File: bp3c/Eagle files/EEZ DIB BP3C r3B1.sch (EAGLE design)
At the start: 56 parts, among them IC1 TCA9534PWR, Q1 2N7002, Q2 2N7002, Q3 2N7002, Q4 2N7002, X1 ZL202-20G, X2 ZL202-20G, X3 ZL202-20G, X4 ZL212-40KG, X5 ZL262-28DG, X6 ZL262-28DG, X7 ZL262-28DG

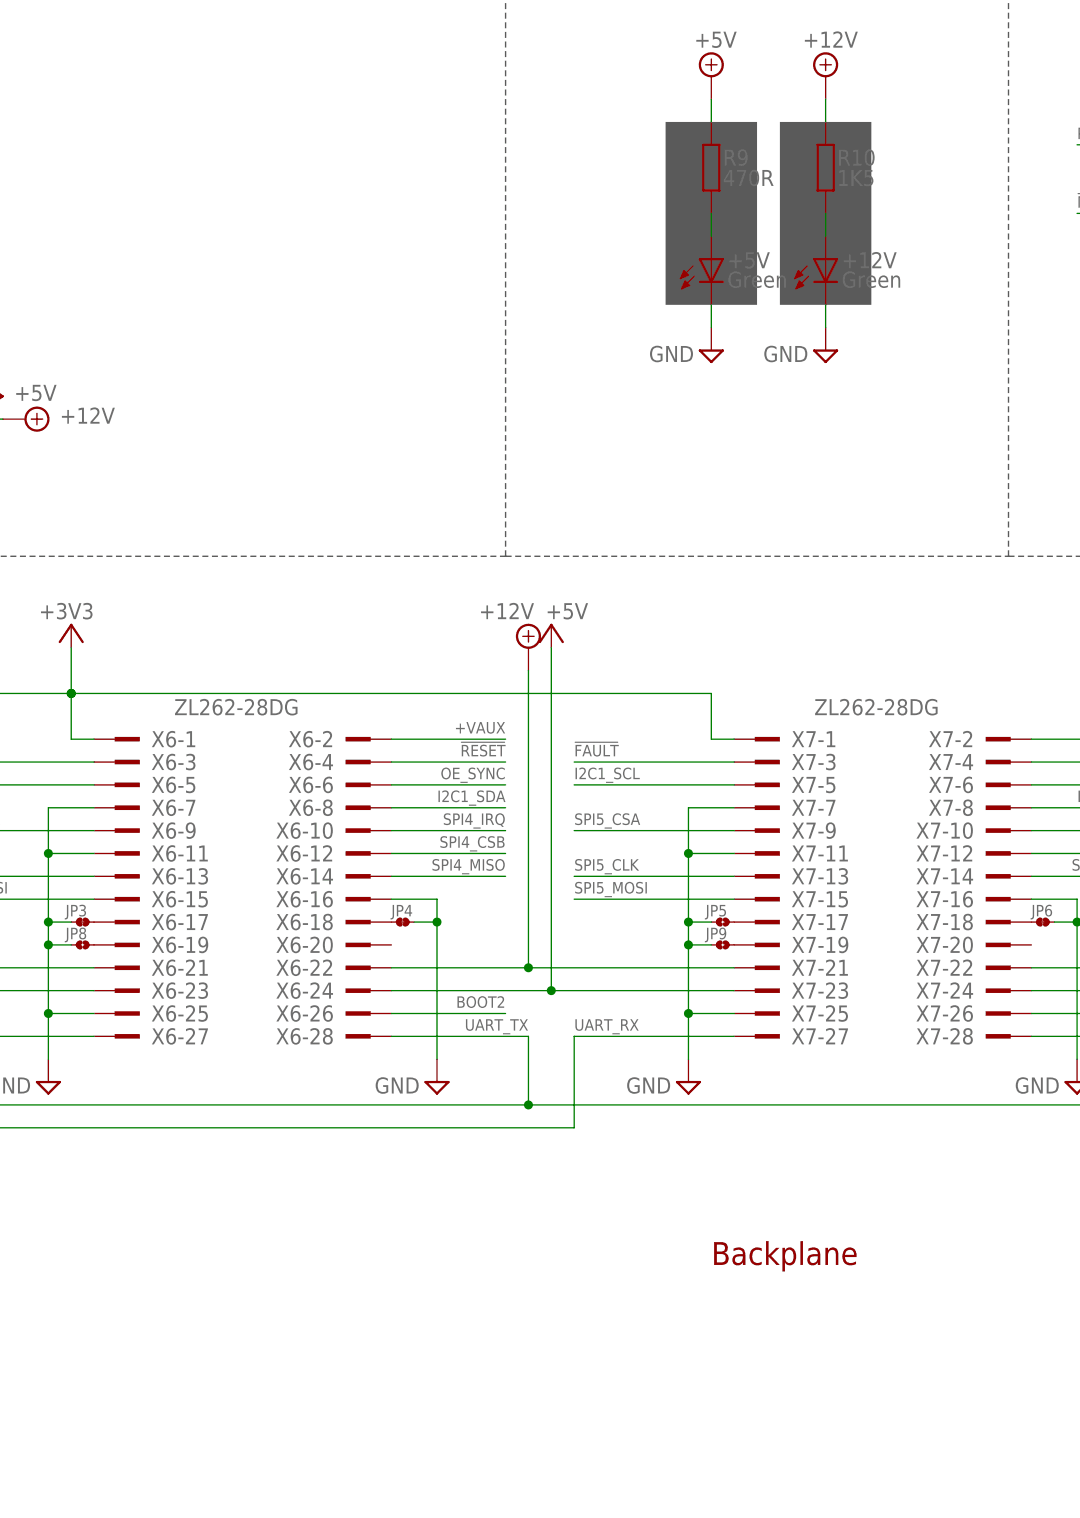
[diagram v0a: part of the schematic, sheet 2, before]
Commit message: BP3C BOM update, optional X8
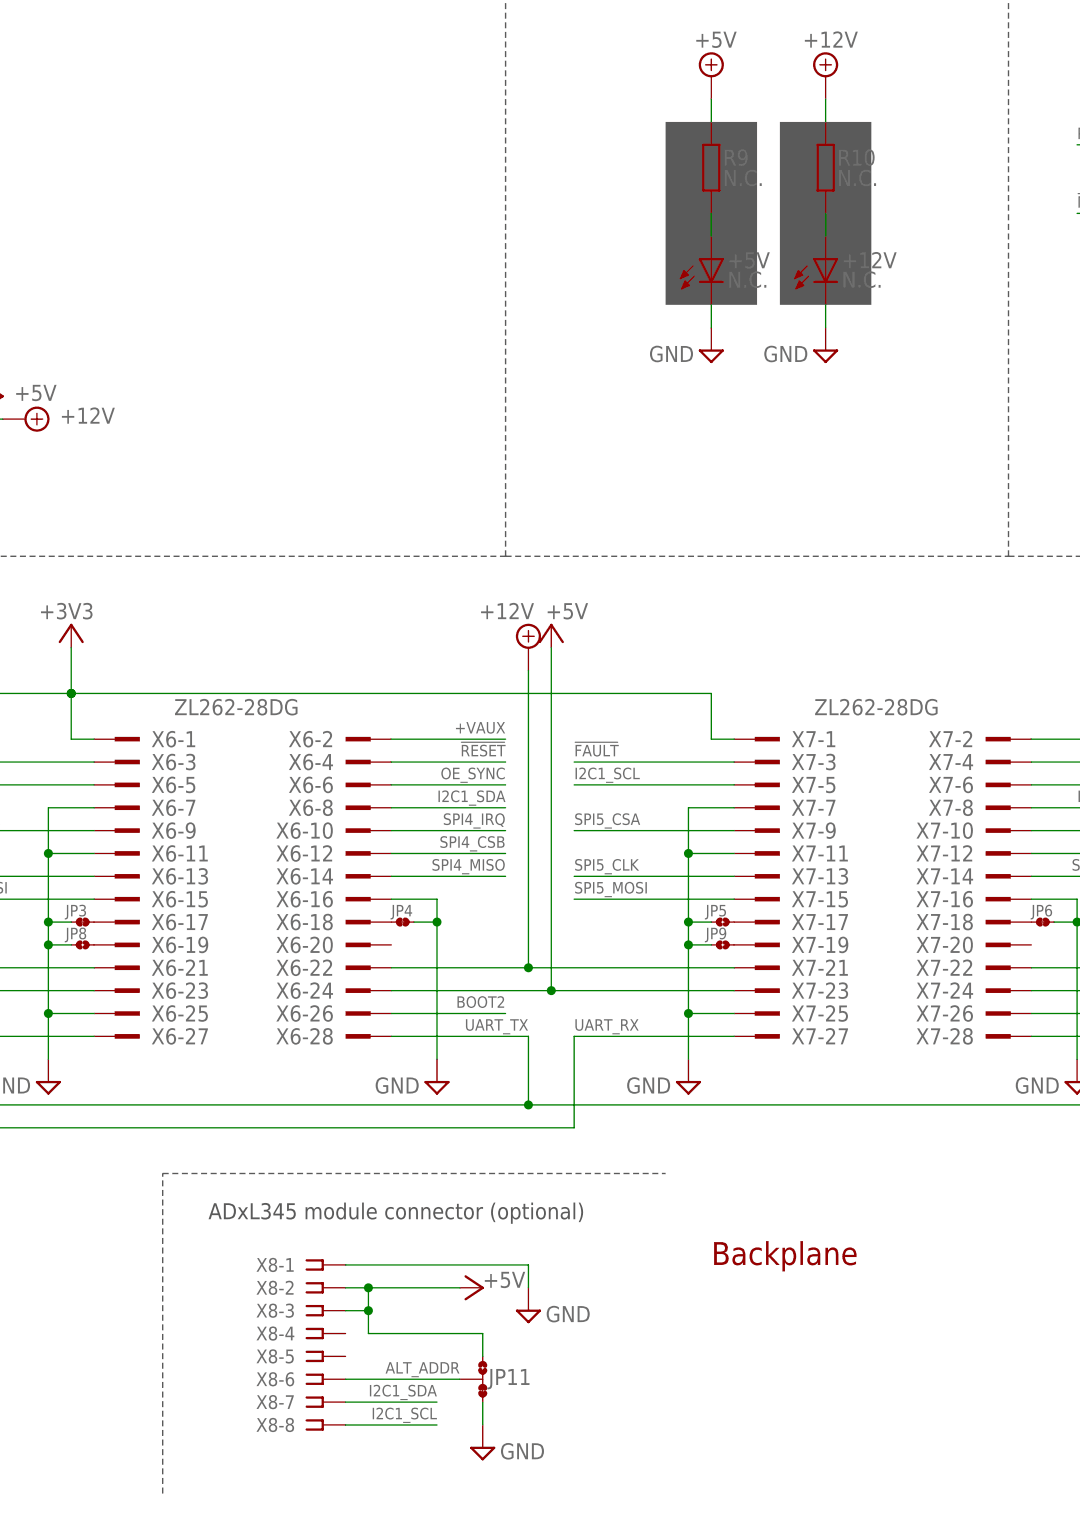
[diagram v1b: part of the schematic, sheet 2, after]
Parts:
- added JP11: JP3-CUT, EEZ_Lib1:JP3-CUT
- added X8: N.C., con-samtec:SSW-108-02-S-S
- +12V, +5V, CGND, SRAIL: value Green -> N.C.
- PAR: value Yellow -> N.C.
- R1, R3, R5, R7: value 330R -> N.C.
- R10: value 1K5 -> N.C.
- R9: value 470R -> N.C.
- SER: value Red -> N.C.
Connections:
- new net ALT_ADDR: JP11.COM, X8-6.1
- net +5V: now also JP11.NO, X8-2.1, X8-3.1
- net GND: now also JP11.NC, X8-1.1
- net I2C1_SCL: now also X8-8.1
- net I2C1_SDA: now also X8-7.1
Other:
- note added: "ADxL345 module connector (optional)"
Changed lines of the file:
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@@
 <part name="P+1" library="supply1" deviceset="+5V" device=""/>
 <part name="P+2" library="supply1" deviceset="+5V" device=""/>
-<part name="SER" library="EEZ_Lib1" deviceset="LED" device="0805" value="Red"/>
-<part name="PAR" library="EEZ_Lib1" deviceset="LED" device="0805" value="Yellow"/>
-<part name="R3" library="rcl" deviceset="R-EU_" device="R0805" value="330R"/>
-<part name="R5" library="rcl" deviceset="R-EU_" device="R0805" value="330R"/>
+<part name="SER" library="EEZ_Lib1" deviceset="LED" device="0805" value="N.C."/>
+<part name="PAR" library="EEZ_Lib1" deviceset="LED" device="0805" value="N.C."/>
+<part name="R3" library="rcl" deviceset="R-EU_" device="R0805" value="N.C."/>
+<part name="R5" library="rcl" deviceset="R-EU_" device="R0805" value="N.C."/>
 <part name="X1" library="EEZ_connectors" deviceset="DS1021-2*10SF11" device="" value="ZL202-20G"/>
 <part name="X2" library="EEZ_connectors" deviceset="DS1021-2*10SF11" device="" value="ZL202-20G"/>
 <part name="X3" library="EEZ_connectors" deviceset="DS1021-2*10SF11" device="" value="ZL202-20G"/>
 <part name="X4" library="EEZ_connectors" deviceset="ZL212-40KG" device=""/>
-<part name="+5V" library="EEZ_Lib1" deviceset="LED" device="0805" value="Green"/>
-<part name="R9" library="rcl" deviceset="R-EU_" device="R0805" value="470R"/>
-<part name="+12V" library="EEZ_Lib1" deviceset="LED" device="0805" value="Green"/>
-<part name="R10" library="rcl" deviceset="R-EU_" device="R0805" value="1K5"/>
+<part name="+5V" library="EEZ_Lib1" deviceset="LED" device="0805" value="N.C."/>
+<part name="R9" library="rcl" deviceset="R-EU_" device="R0805" value="N.C."/>
+<part name="+12V" library="EEZ_Lib1" deviceset="LED" device="0805" value="N.C."/>
+<part name="R10" library="rcl" deviceset="R-EU_" device="R0805" value="N.C."/>
 <part name="SUPPLY3" library="supply2" deviceset="+12V" device=""/>
 <part name="SUPPLY32" library="supply2" deviceset="+5V" device=""/>
@@
 <part name="R2" library="rcl" deviceset="R-EU_" device="R0805" value="100K"/>
 <part name="P+3" library="supply1" deviceset="+5V" device=""/>
-<part name="CGND" library="EEZ_Lib1" deviceset="LED" device="0805" value="Green"/>
-<part name="R1" library="rcl" deviceset="R-EU_" device="R0805" value="330R"/>
+<part name="CGND" library="EEZ_Lib1" deviceset="LED" device="0805" value="N.C."/>
+<part name="R1" library="rcl" deviceset="R-EU_" device="R0805" value="N.C."/>
 <part name="K_SRAIL" library="EEZ_Lib1" deviceset="RELAY_RT314012" device="-2" value="RT424005"/>
 <part name="D6" library="EEZ_Lib1" deviceset="DIODE" device="SOD323R" value="BAS316"/>
@@
 <part name="R8" library="rcl" deviceset="R-EU_" device="R0805" value="100K"/>
 <part name="P+8" library="supply1" deviceset="+5V" device=""/>
-<part name="SRAIL" library="EEZ_Lib1" deviceset="LED" device="0805" value="Green"/>
-<part name="R7" library="rcl" deviceset="R-EU_" device="R0805" value="330R"/>
+<part name="SRAIL" library="EEZ_Lib1" deviceset="LED" device="0805" value="N.C."/>
+<part name="R7" library="rcl" deviceset="R-EU_" device="R0805" value="N.C."/>
 <part name="D4" library="EEZ_Lib1" deviceset="DIODE" device="SOD323R" value="N.C."/>
 <part name="D3" library="EEZ_Lib1" deviceset="DIODE" device="SOD323R" value="N.C."/>
@@
 <part name="R11" library="rcl" deviceset="R-EU_" device="R0805" value="10K"/>
 <part name="+3V4" library="supply1" deviceset="+3V3" device=""/>
+<part name="X8" library="con-samtec" deviceset="SSW-108-02-S-S" device="" value="N.C."/>
+<part name="SUPPLY20" library="supply2" deviceset="GND" device=""/>
+<part name="P+11" library="supply1" deviceset="+5V" device=""/>
+<part name="JP11" library="EEZ_Lib1" deviceset="JP3-CUT" device=""/>
+<part name="SUPPLY21" library="supply2" deviceset="GND" device=""/>
 </parts>
 <sheets>
@@
 <vertex x="98.425" y="165.1"/>
 <vertex x="104.775" y="165.1"/>
-<vertex x="102.235" y="146.05"/>
+<vertex x="104.775" y="146.05"/>
 <vertex x="88.9" y="146.05"/>
 </polygon>
@@
 <wire x1="198.12" y1="106.68" x2="198.12" y2="177.8" width="0.1524" layer="97" style="shortdash"/>
 <text x="205.74" y="175.26" size="1.778" layer="97">Peripheral modules RESET</text>
+<wire x1="104.14" y1="38.1" x2="160.02" y2="38.1" width="0.1524" layer="97" style="shortdash"/>
+<wire x1="104.14" y1="2.54" x2="104.14" y2="38.1" width="0.1524" layer="97" style="shortdash"/>
+<text x="109.22" y="33.02" size="1.778" layer="97">ADxL345 module connector (optional)</text>
 </plain>
 <instances>
@@
 <attribute name="VALUE" x="230.505" y="172.72" size="1.778" layer="96" rot="MR180"/>
 </instance>
+<instance part="X8" gate="-1" x="121.92" y="27.94" smashed="yes">
+<attribute name="NAME" x="118.872" y="28.702" size="1.524" layer="95" rot="R180"/>
+</instance>
+<instance part="X8" gate="-2" x="121.92" y="25.4" smashed="yes">
+<attribute name="NAME" x="118.872" y="26.162" size="1.524" layer="95" rot="R180"/>
+</instance>
+<instance part="X8" gate="-3" x="121.92" y="22.86" smashed="yes">
+<attribute name="NAME" x="118.872" y="23.622" size="1.524" layer="95" rot="R180"/>
+</instance>
+<instance part="X8" gate="-4" x="121.92" y="20.32" smashed="yes">
+<attribute name="NAME" x="118.872" y="21.082" size="1.524" layer="95" rot="R180"/>
+</instance>
+<instance part="X8" gate="-5" x="121.92" y="17.78" smashed="yes">
+<attribute name="NAME" x="118.872" y="18.542" size="1.524" layer="95" rot="R180"/>
+</instance>
+<instance part="X8" gate="-6" x="121.92" y="15.24" smashed="yes">
+<attribute name="NAME" x="118.872" y="16.002" size="1.524" layer="95" rot="R180"/>
+</instance>
+<instance part="X8" gate="-7" x="121.92" y="12.7" smashed="yes">
+<attribute name="NAME" x="118.872" y="13.462" size="1.524" layer="95" rot="R180"/>
+</instance>
+<instance part="X8" gate="-8" x="121.92" y="10.16" smashed="yes">
+<attribute name="NAME" x="118.872" y="10.922" size="1.524" layer="95" rot="R180"/>
+</instance>
+<instance part="SUPPLY20" gate="GND" x="144.78" y="22.86" smashed="yes" rot="MR0">
+<attribute name="VALUE" x="146.685" y="21.59" size="1.778" layer="96"/>
+</instance>
+<instance part="P+11" gate="1" x="139.7" y="25.4" smashed="yes" rot="R270">
+<attribute name="VALUE" x="139.7" y="25.4" size="1.778" layer="96"/>
+</instance>
+<instance part="JP11" gate="G$1" x="139.7" y="15.24" smashed="yes" rot="MR0">
+<attribute name="NAME" x="140.335" y="14.605" size="1.778" layer="95"/>
+</instance>
+<instance part="SUPPLY21" gate="GND" x="139.7" y="7.62" smashed="yes" rot="MR0">
+<attribute name="VALUE" x="141.605" y="6.35" size="1.778" layer="96"/>
+</instance>
 </instances>
 <busses>
@@
 <pinref part="X5" gate="-16" pin="1"/>
 </segment>
+<segment>
+<pinref part="X8" gate="-1" pin="1"/>
+<wire x1="124.46" y1="27.94" x2="144.78" y2="27.94" width="0.1524" layer="91"/>
+<pinref part="SUPPLY20" gate="GND" pin="GND"/>
+<wire x1="144.78" y1="25.4" x2="144.78" y2="27.94" width="0.1524" layer="91"/>
+</segment>
+<segment>
+<pinref part="SUPPLY21" gate="GND" pin="GND"/>
+<pinref part="JP11" gate="G$1" pin="NC"/>
+<wire x1="139.7" y1="10.16" x2="139.7" y2="12.7" width="0.1524" layer="91"/>
+</segment>
 </net>
 <net name="+3V3" class="0">
@@
 <pinref part="X7" gate="-24" pin="1"/>
 </segment>
+<segment>
+<pinref part="X8" gate="-2" pin="1"/>
+<wire x1="124.46" y1="25.4" x2="127" y2="25.4" width="0.1524" layer="91"/>
+<pinref part="P+11" gate="1" pin="+5V"/>
+<pinref part="X8" gate="-3" pin="1"/>
+<wire x1="127" y1="25.4" x2="137.16" y2="25.4" width="0.1524" layer="91"/>
+<wire x1="124.46" y1="22.86" x2="127" y2="22.86" width="0.1524" layer="91"/>
+<wire x1="127" y1="22.86" x2="127" y2="25.4" width="0.1524" layer="91"/>
+<junction x="127" y="25.4"/>
+<pinref part="JP11" gate="G$1" pin="NO"/>
+<wire x1="139.7" y1="17.78" x2="139.7" y2="20.32" width="0.1524" layer="91"/>
+<wire x1="139.7" y1="20.32" x2="127" y2="20.32" width="0.1524" layer="91"/>
+<wire x1="127" y1="20.32" x2="127" y2="22.86" width="0.1524" layer="91"/>
+<junction x="127" y="22.86"/>
+</segment>
 </net>
 <net name="+12V" class="0">
@@
 <pinref part="X7" gate="-8" pin="1"/>
 </segment>
+<segment>
+<pinref part="X8" gate="-7" pin="1"/>
+<wire x1="124.46" y1="12.7" x2="134.62" y2="12.7" width="0.1524" layer="91"/>
+<label x="134.62" y="13.335" size="1.27" layer="102" rot="MR0"/>
+</segment>
 </net>
 <net name="I2C1_SCL" class="0">
@@
 <label x="149.86" y="83.185" size="1.27" layer="102" rot="MR180"/>
 <pinref part="X7" gate="-5" pin="1"/>
+</segment>
+<segment>
+<wire x1="124.46" y1="10.16" x2="134.62" y2="10.16" width="0.1524" layer="91"/>
+<label x="134.62" y="10.795" size="1.27" layer="102" rot="MR0"/>
+<pinref part="X8" gate="-8" pin="1"/>
 </segment>
 </net>
@@
 </segment>
 </net>
+<net name="ALT_ADDR" class="0">
+<segment>
+<pinref part="X8" gate="-6" pin="1"/>
+<wire x1="124.46" y1="15.24" x2="137.16" y2="15.24" width="0.1524" layer="91"/>
+<label x="137.16" y="15.875" size="1.27" layer="102" rot="MR0"/>
+<pinref part="JP11" gate="G$1" pin="COM"/>
+</segment>
+</net>

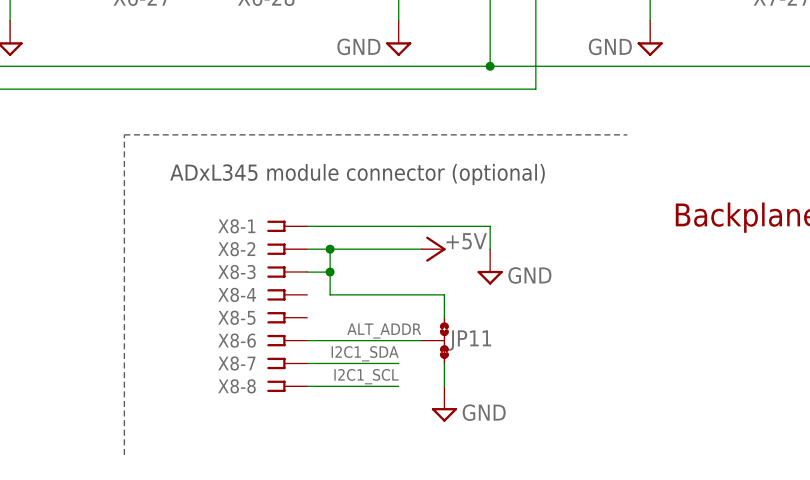
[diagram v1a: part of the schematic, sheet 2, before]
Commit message: BP3C ADXL module CS fixed
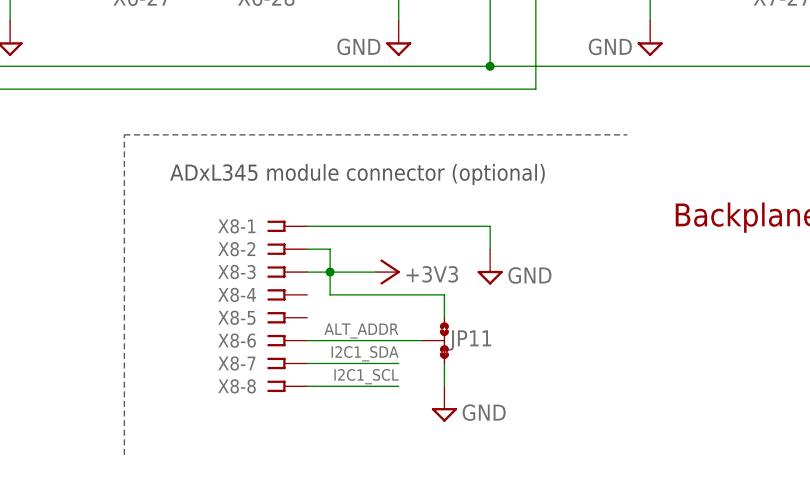
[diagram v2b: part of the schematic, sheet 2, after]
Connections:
- net +3V3: now also JP11.NO, X8-2.1, X8-3.1
- net +5V: no longer JP11.NO, X8-2.1, X8-3.1
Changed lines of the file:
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@@
 <part name="X8" library="con-samtec" deviceset="SSW-108-02-S-S" device="" value="N.C."/>
 <part name="SUPPLY20" library="supply2" deviceset="GND" device=""/>
-<part name="P+11" library="supply1" deviceset="+5V" device=""/>
 <part name="JP11" library="EEZ_Lib1" deviceset="JP3-CUT" device=""/>
 <part name="SUPPLY21" library="supply2" deviceset="GND" device=""/>
+<part name="+3V5" library="supply1" deviceset="+3V3" device=""/>
 </parts>
 <sheets>
@@
 <attribute name="VALUE" x="146.685" y="21.59" size="1.778" layer="96"/>
 </instance>
-<instance part="P+11" gate="1" x="139.7" y="25.4" smashed="yes" rot="R270">
-<attribute name="VALUE" x="139.7" y="25.4" size="1.778" layer="96"/>
-</instance>
 <instance part="JP11" gate="G$1" x="139.7" y="15.24" smashed="yes" rot="MR0">
 <attribute name="NAME" x="140.335" y="14.605" size="1.778" layer="95"/>
@@
 <instance part="SUPPLY21" gate="GND" x="139.7" y="7.62" smashed="yes" rot="MR0">
 <attribute name="VALUE" x="141.605" y="6.35" size="1.778" layer="96"/>
+</instance>
+<instance part="+3V5" gate="G$1" x="134.62" y="22.86" smashed="yes" rot="R270">
+<attribute name="VALUE" x="135.255" y="23.495" size="1.778" layer="96" rot="MR180"/>
 </instance>
 </instances>
@@
 <wire x1="233.68" y1="167.64" x2="233.68" y2="165.1" width="0.1524" layer="91"/>
 </segment>
+<segment>
+<pinref part="X8" gate="-3" pin="1"/>
+<wire x1="124.46" y1="22.86" x2="127" y2="22.86" width="0.1524" layer="91"/>
+<pinref part="JP11" gate="G$1" pin="NO"/>
+<wire x1="139.7" y1="17.78" x2="139.7" y2="20.32" width="0.1524" layer="91"/>
+<wire x1="139.7" y1="20.32" x2="127" y2="20.32" width="0.1524" layer="91"/>
+<wire x1="127" y1="20.32" x2="127" y2="22.86" width="0.1524" layer="91"/>
+<wire x1="127" y1="22.86" x2="132.08" y2="22.86" width="0.1524" layer="91"/>
+<junction x="127" y="22.86"/>
+<pinref part="+3V5" gate="G$1" pin="+3V3"/>
+<pinref part="X8" gate="-2" pin="1"/>
+<wire x1="124.46" y1="25.4" x2="127" y2="25.4" width="0.1524" layer="91"/>
+<wire x1="127" y1="25.4" x2="127" y2="22.86" width="0.1524" layer="91"/>
+</segment>
 </net>
 <net name="!FAULT" class="0">
@@
 <wire x1="215.9" y1="58.42" x2="200.66" y2="58.42" width="0.1524" layer="91"/>
 <pinref part="X7" gate="-24" pin="1"/>
-</segment>
-<segment>
-<pinref part="X8" gate="-2" pin="1"/>
-<wire x1="124.46" y1="25.4" x2="127" y2="25.4" width="0.1524" layer="91"/>
-<pinref part="P+11" gate="1" pin="+5V"/>
-<pinref part="X8" gate="-3" pin="1"/>
-<wire x1="127" y1="25.4" x2="137.16" y2="25.4" width="0.1524" layer="91"/>
-<wire x1="124.46" y1="22.86" x2="127" y2="22.86" width="0.1524" layer="91"/>
-<wire x1="127" y1="22.86" x2="127" y2="25.4" width="0.1524" layer="91"/>
-<junction x="127" y="25.4"/>
-<pinref part="JP11" gate="G$1" pin="NO"/>
-<wire x1="139.7" y1="17.78" x2="139.7" y2="20.32" width="0.1524" layer="91"/>
-<wire x1="139.7" y1="20.32" x2="127" y2="20.32" width="0.1524" layer="91"/>
-<wire x1="127" y1="20.32" x2="127" y2="22.86" width="0.1524" layer="91"/>
-<junction x="127" y="22.86"/>
 </segment>
 </net>
@@
 <pinref part="X8" gate="-6" pin="1"/>
 <wire x1="124.46" y1="15.24" x2="137.16" y2="15.24" width="0.1524" layer="91"/>
-<label x="137.16" y="15.875" size="1.27" layer="102" rot="MR0"/>
+<label x="134.62" y="15.875" size="1.27" layer="102" rot="MR0"/>
 <pinref part="JP11" gate="G$1" pin="COM"/>
 </segment>
